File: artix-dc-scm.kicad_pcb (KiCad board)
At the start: 8 copper layers, 90 x 120.4 mm, 342 parts, among them IC1 TPS54561, J1 WE-RJ45_7499111121A, J10 61300611121, J11 DC_SOCKET, J12 S2B-PH-K-S_LF__SN_, J13 62000311121, J2 1-2199230-6, J3 543630489, J4 M20-7830642, J5 SFF-TA-1002-4C+, J6 0878311420, J7 61301021121, J8 61301021121, J9 61301221121, Q1 IRLML6402TRPBF, Q10 2N7002, Q11 2N7002, Q2 IRLML6402TRPBF, Q3 IRLML6402TRPBF, Q4 IRLML6402TRPBF, Q5 IRLML6402TRPBF, Q6 IRLML6402TRPBF, Q7 2N7002, Q8 2N7002, Q9 2N7002, U1 KSZ9031RNXCA, U10 TPS62823DLCT, U11 TPS62823DLCT, U12 TPS62823DLCT, U13 TPS62823DLCT, U14 XC7A100T-FGG484, U15 SN74LVC1G08DCKR, U15 TPS62823DLCT, U16 SN74LS08DBR, U2 W25Q32JVSSIQ_TR, U3 W25Q32JVSSIQ_TR, U4 W25Q32JVSSIQ_TR, U5 W25Q32JVSSIQ_TR, U6 NVT2008DQ,115, U7 AS4C256M16D3, U8 TPS51200DRC, U9 LM3881MME_NOPB, Y1 ABM8G-25.000MHZ-18-D2Y-T

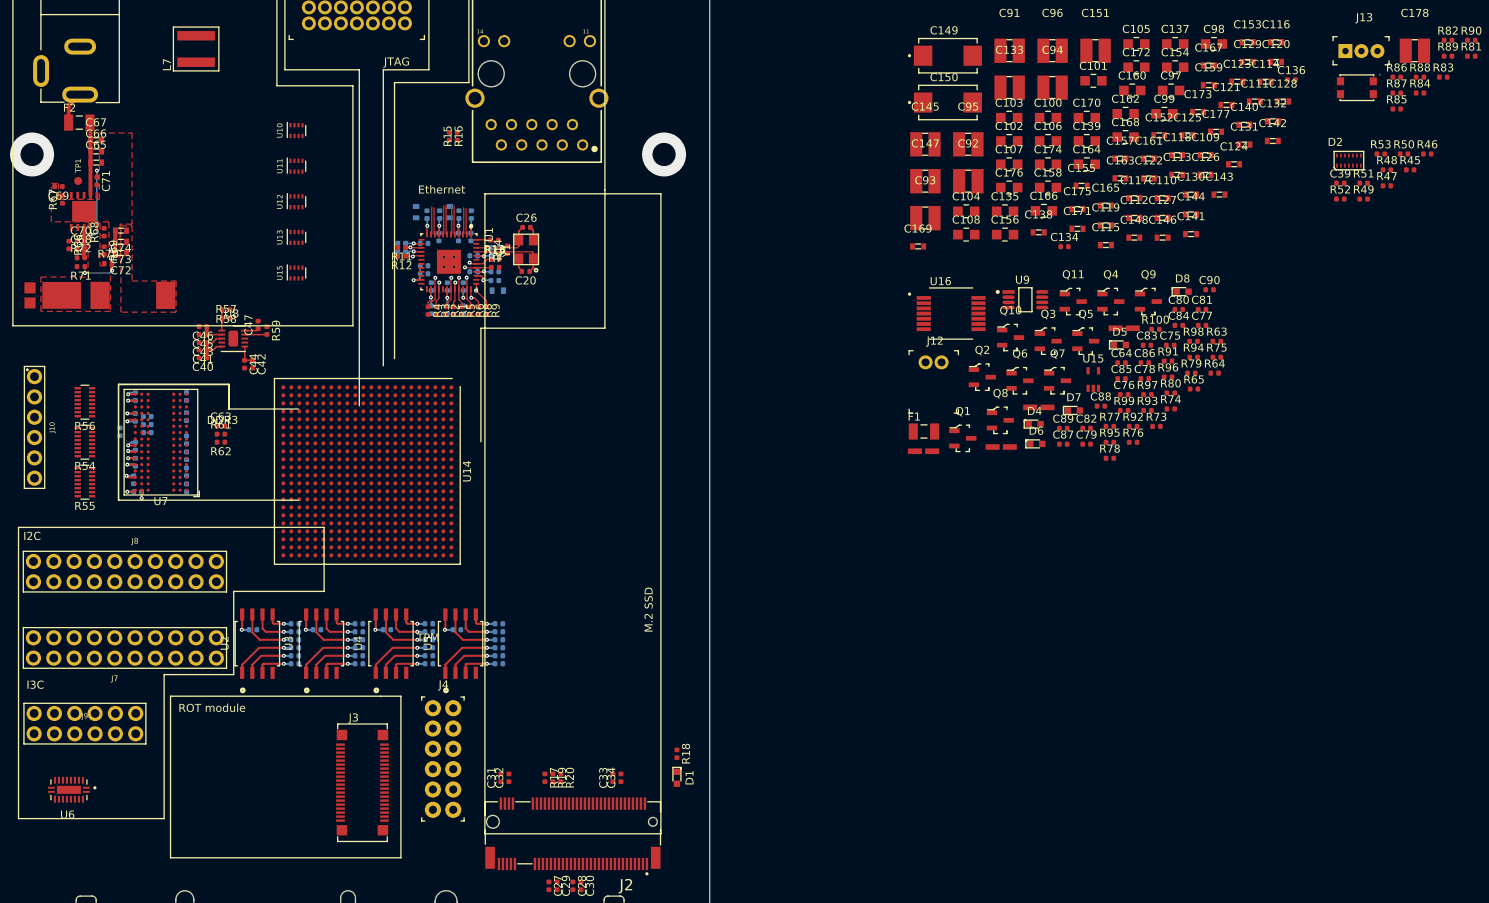
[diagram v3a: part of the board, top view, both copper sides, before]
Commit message: Added interfaces layouts
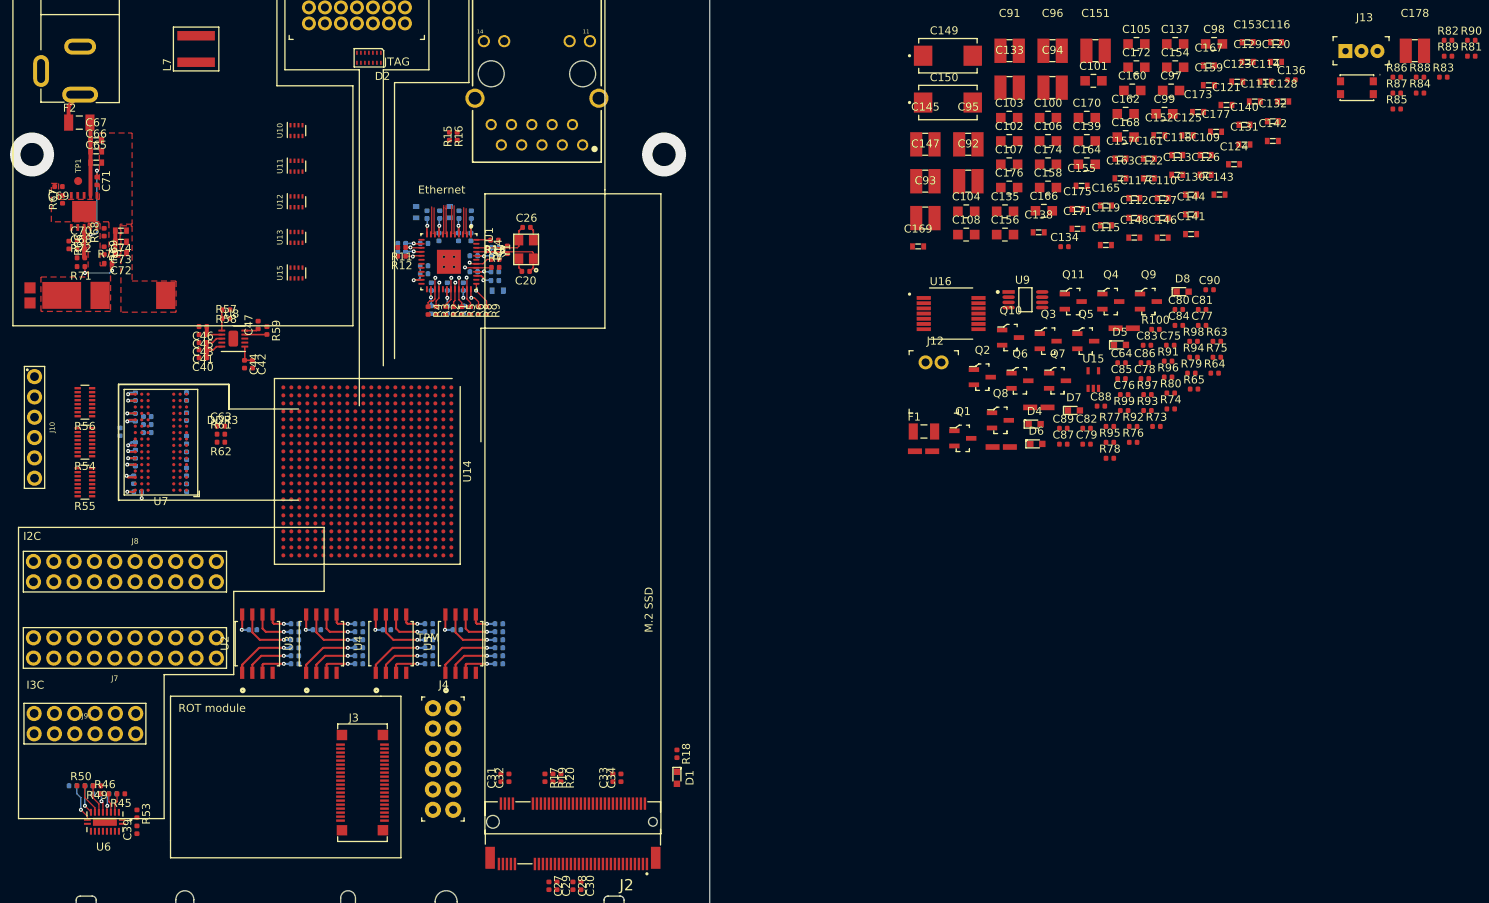
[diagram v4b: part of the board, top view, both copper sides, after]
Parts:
- R47, R48, R51, R52: moved to B.Cu
- moved R46 183.6 mm to (74.5, 160.0)
- moved R50 183.3 mm to (71.5, 159.0)
- moved R48 179.1 mm to (73.5, 160.0)
- moved R45 179.0 mm to (76.5, 160.0), turned to 180 degrees
- moved R47 176.5 mm to (75.5, 160.0), turned to 180 degrees
- moved R51 176.2 mm to (72.5, 159.0), turned to 180 degrees
- moved R53 176.0 mm to (78.5, 162.5), turned to 270 degrees
- moved R52 174.6 mm to (70.5, 159.0)
- moved R49 174.5 mm to (73.5, 159.0), turned to 180 degrees
- moved C39 170.8 mm to (78.5, 164.5), turned to 90 degrees
- moved D2 123.2 mm to (107.5, 68.0), turned to 180 degrees
- moved U6 6.02 mm to (74.5, 163.5)
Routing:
- net I3C[3]_SCL_3V3: track 0.00 -> 4.80 mm, vias 0 -> 1
- net I3C[2]_SCL_3V3: track 0.00 -> 3.84 mm
- net I3C[3]_SDA_3V3: track 0.00 -> 3.63 mm, vias 0 -> 1
- net I3C[2]_SDA_3V3: track 0.00 -> 3.62 mm
- net I3C[1]_SCL_3V3: track 0.00 -> 2.42 mm, vias 0 -> 1
- net I3C[0]_SDA_3V3: track 0.00 -> 2.42 mm
- net I3C[0]_SCL_3V3: track 0.00 -> 2.42 mm
- net I3C[1]_SDA_3V3: track 0.00 -> 2.42 mm, vias 0 -> 1

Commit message: Add local component libraries
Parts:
- C1, C10, C11, C12, C13, C134, C136, C14, C15, C16, C17, C18, C19, C2, C20, C21, C22, C23, C24, C25, C26, C27, C28, C29, C3, C30, C31, C32, C33, C34, C35, C36, C37, C38, C39, C4, C40, C41, C42, C43, C44, C45, C46, C47, C48, C49, C5, C50, C51, C52, C53, C54, C55, C56, C57, C58, C59, C6, C60, C61, C62, C63, C64, C68, C69, C7, C70, C71, C75, C76, C77, C78, C8, C83, C84, C85, C86, C87, C88, C89, C9, C90: footprint antmicro-footprints:0402-cap -> artix-dc-scm-footprints:0402-cap
- C100, C101, C102, C103, C104, C105, C106, C107, C108, C135, C137, C139, C154, C156, C158, C160, C162, C164, C166, C168, C170, C172, C174, C176, C97, C98, C99: footprint antmicro-footprints:0805-cap -> artix-dc-scm-footprints:0805-cap
- C109, C110, C111, C112, C113, C114, C115, C116, C117, C118, C119, C120, C121, C122, C123, C124, C125, C126, C127, C128, C129, C130, C131, C132, C138, C140, C141, C142, C143, C144, C146, C148, C152, C153, C155, C157, C159, C161, C163, C165, C167, C169, C171, C173, C175, C177, C65, C66, C67, C72, C73, C74: footprint antmicro-footprints:0603-cap -> artix-dc-scm-footprints:0603-cap
- C133, C145, C147, C151, C178, C91, C92, C93, C94, C95, C96: footprint antmicro-footprints:1210-cap -> artix-dc-scm-footprints:1210-cap
- C149, C150: footprint antmicro-footprints:KEMET_D -> artix-dc-scm-footprints:KEMET_D
- C79, C80, C81, C82, R1, R10, R100, R11, R12, R13, R14, R15, R16, R17, R18, R19, R2, R20, R21, R22, R23, R24, R25, R26, R27, R28, R29, R3, R30, R31, R32, R33, R34, R35, R36, R37, R38, R39, R4, R40, R41, R42, R43, R44, R45, R46, R47, R48, R49, R5, R50, R51, R52, R53, R57, R58, R59, R6, R60, R61, R62, R63, R64, R65, R66, R67, R68, R69, R7, R70, R71, R72, R73, R74, R75, R76, R77, R78, R79, R8, R80, R81, R82, R83, R84, R85, R86, R87, R88, R89, R9, R90, R91, R92, R93, R94, R95, R96, R97, R98, R99: footprint antmicro-footprints:0402-res -> artix-dc-scm-footprints:0402-res
- D1, D4, D5, D6, D7, D8: footprint antmicro-footprints:LED_0603 -> artix-dc-scm-footprints:LED_0603
- D2: footprint antmicro-footprints:TPD6E05U06 -> artix-dc-scm-footprints:TPD6E05U06
- D3: footprint antmicro-footprints:PDS760-13 -> artix-dc-scm-footprints:PDS760-13
- F1, F2: footprint antmicro-footprints:1206-Fuse-Littelfuse-0466-0-0-MFG -> artix-dc-scm-footprints:1206-Fuse-Littelfuse-0466-0-0-MFG
- FB1, FB2, FB3: footprint antmicro-footprints:0603-res -> artix-dc-scm-footprints:0603-res
- IC1: footprint antmicro-footprints:WSON-10_4x4 -> artix-dc-scm-footprints:WSON-10_4x4
- J1: footprint antmicro-footprints:7499111121A -> artix-dc-scm-footprints:7499111121A
- J10: footprint antmicro-footprints:61300611121 -> artix-dc-scm-footprints:61300611121
- J11: footprint antmicro-footprints:DC_SOCKET -> artix-dc-scm-footprints:DC_SOCKET
- J12: footprint antmicro-footprints:PinHeader_1x2_P2mm_Drill1mm_RA -> artix-dc-scm-footprints:PinHeader_1x2_P2mm_Drill1mm_RA
- J13: footprint antmicro-footprints:62000311121 -> artix-dc-scm-footprints:62000311121
- J2: footprint antmicro-footprints:1-2199230-6 -> artix-dc-scm-footprints:1-2199230-6
- J3: footprint antmicro-footprints:543630489 -> artix-dc-scm-footprints:543630489
- J4: footprint antmicro-footprints:PinHeader_6x2_P2.54mm_Vertical -> artix-dc-scm-footprints:PinHeader_6x2_P2.54mm_Vertical
- J5: footprint antmicro-footprints:SFF-TA-1002-4C+ -> artix-dc-scm-footprints:SFF-TA-1002-4C+
- J6: footprint antmicro-footprints:PinHeader_2x7_P2mm_Drill1mm -> artix-dc-scm-footprints:PinHeader_2x7_P2mm_Drill1mm
- J7, J8: footprint antmicro-footprints:61301021121 -> artix-dc-scm-footprints:61301021121
- J9: footprint antmicro-footprints:61301221121 -> artix-dc-scm-footprints:61301221121
- L1: footprint antmicro-footprints:WE_7447798720 -> artix-dc-scm-footprints:WE_7447798720
- L2, L3, L4, L5: footprint antmicro-footprints:IHLP-1212AE -> artix-dc-scm-footprints:IHLP-1212AE
- L7: footprint antmicro-footprints:Coilcraft-XAL5030 -> artix-dc-scm-footprints:Coilcraft-XAL5030
- Q1, Q10, Q11, Q2, Q3, Q4, Q5, Q6, Q7, Q8, Q9: footprint antmicro-footprints:SOT-23-3 -> artix-dc-scm-footprints:SOT-23-3
- R54, R55, R56: footprint antmicro-footprints:R_Array_Convex_8x0602 -> artix-dc-scm-footprints:R_Array_Convex_8x0602
- S1: footprint antmicro-footprints:SW_SPST_4.2x2.8 -> artix-dc-scm-footprints:SW_SPST_4.2x2.8
- TP1: footprint antmicro-footprints:Testpoint_smd_1mm -> artix-dc-scm-footprints:Testpoint_smd_1mm
- U1: footprint antmicro-footprints:QFN-48-Microchip-QFN77-48LD-PL-2 -> artix-dc-scm-footprints:QFN-48-Microchip-QFN77-48LD-PL-2
- U10, U11, U12, U13, U15: footprint antmicro-footprints:QFN-8_2x1mm -> artix-dc-scm-footprints:QFN-8_2x1mm
- U14: footprint antmicro-footprints:Xilinx_FGG484 -> artix-dc-scm-footprints:Xilinx_FGG484
- U15: footprint antmicro-footprints:SC-70-5 -> artix-dc-scm-footprints:SC-70-5
- U16: footprint antmicro-footprints:SOP65P775X265-14N -> artix-dc-scm-footprints:SOP65P775X265-14N
- U2, U3, U4, U5: footprint antmicro-footprints:W25Q32JVSSIQ -> artix-dc-scm-footprints:W25Q32JVSSIQ
- U6: footprint antmicro-footprints:QFN50P250X450X100-21N -> artix-dc-scm-footprints:QFN50P250X450X100-21N
- U7: footprint antmicro-footprints:BGA-96_9.0x13.0mm_Layout2x3x16_P0.8mm -> artix-dc-scm-footprints:BGA-96_9.0x13.0mm_Layout2x3x16_P0.8mm
- U8: footprint antmicro-footprints:VSON-10-1EP_3x3mm -> artix-dc-scm-footprints:VSON-10-1EP_3x3mm
- U9: footprint antmicro-footprints:VSSOP8-Texas_Instruments-DGK0008A -> artix-dc-scm-footprints:VSSOP8-Texas_Instruments-DGK0008A
- Y1: footprint antmicro-footprints:KX-7 -> artix-dc-scm-footprints:KX-7

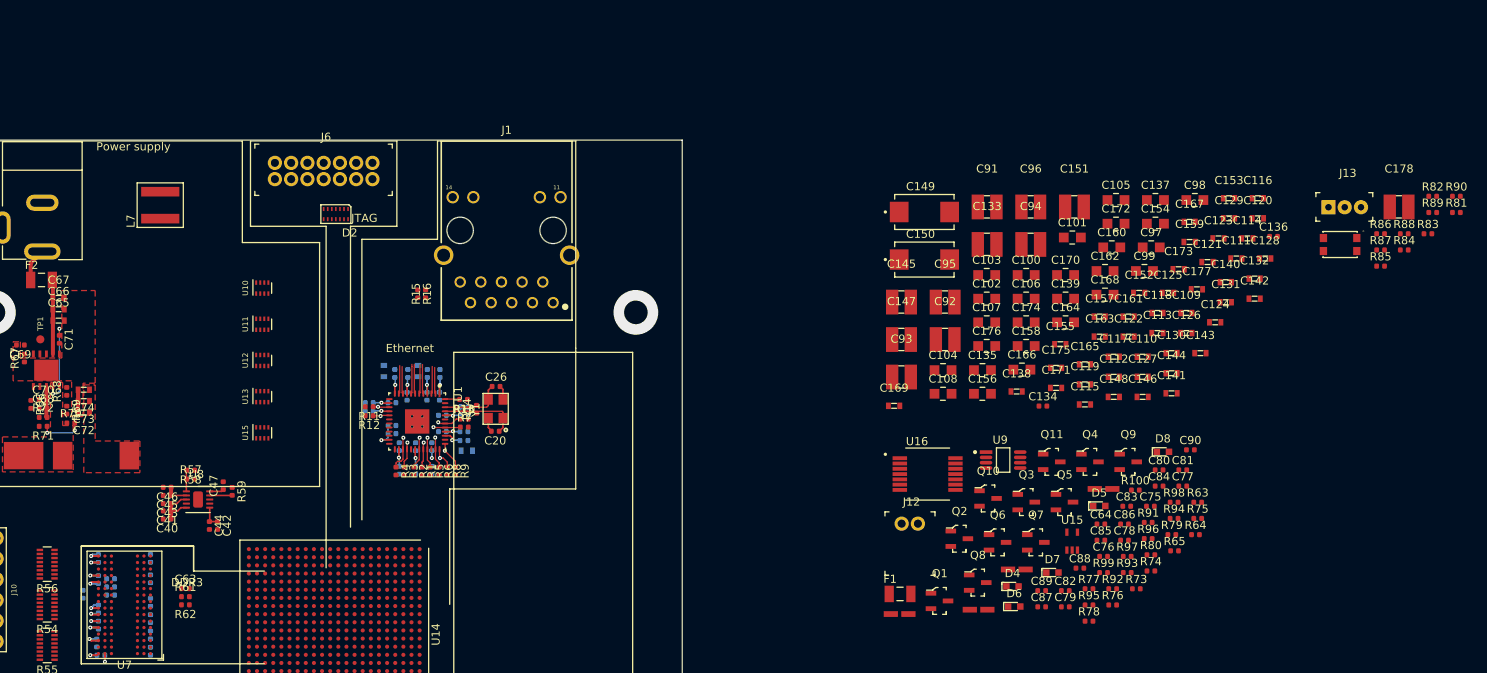
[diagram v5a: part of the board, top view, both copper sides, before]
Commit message: Added VRs component placement, fix in 5V0 layout
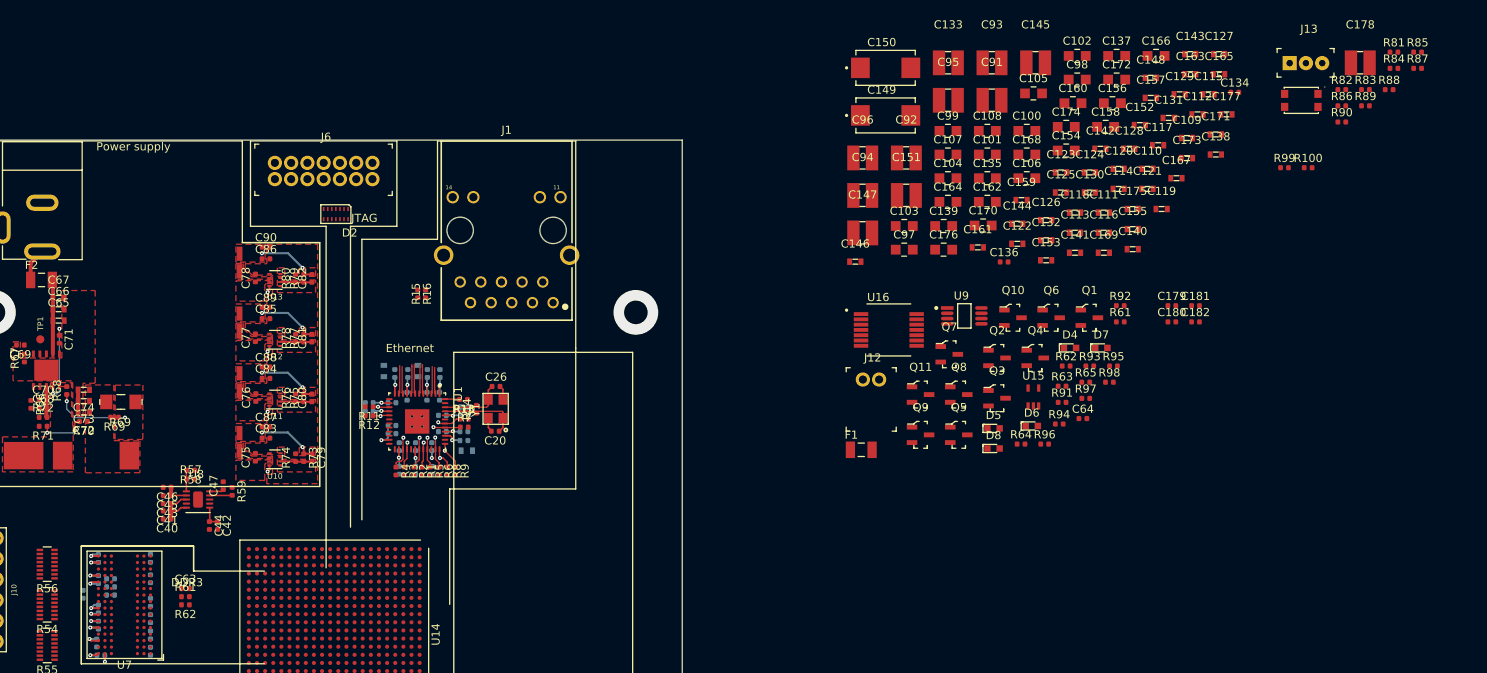
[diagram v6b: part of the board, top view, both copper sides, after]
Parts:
- removed L7: XAL5030-801, artix-dc-scm-footprints:Coilcraft-XAL5030
- removed the R69 at (74.4, 92.1)
- removed the U15 at (198.1, 108.2)
- removed the U15 at (98.5, 94.9)
- added C179: C_100n_0402, artix-dc-scm-footprints:0402-cap, F.Cu at (210.3, 79.3)
- added C180: C_100n_0402, artix-dc-scm-footprints:0402-cap, F.Cu at (210.3, 81.3)
- added C181: C_100n_0402, artix-dc-scm-footprints:0402-cap, F.Cu at (213.2, 79.3)
- added C182: C_100n_0402, artix-dc-scm-footprints:0402-cap, F.Cu at (213.2, 81.3)
- added R61: R_10k_0402, artix-dc-scm-footprints:0402-res, F.Cu at (204.0, 81.3)
- added R62: R_10k_0402, artix-dc-scm-footprints:0402-res, F.Cu at (197.3, 86.7)
- added R69: R_0R_1206, artix-dc-scm-footprints:1206-res, F.Cu at (81.1, 91.1)
- added R69: R_0R_0402, artix-dc-scm-footprints:0402-res, F.Cu at (80.3, 93.0)
- added U15: SN74LVC1G08DCKR, artix-dc-scm-footprints:SC-70-5, F.Cu at (193.3, 90.5)
- R100, R99: value R_1k_0402 -> R_51R_0402
- R94, R95: value R_10k_0402 -> R_1k_0402
- moved C90 116.4 mm to (98.9, 72.1)
- moved C77 115.5 mm to (97.6, 83.2), turned to 90 degrees
- moved C78 111.6 mm to (97.6, 75.9), turned to 90 degrees
- moved R79 111.3 mm to (103.6, 75.9), turned to 90 degrees
- moved R75 110.9 mm to (103.6, 90.6), turned to 90 degrees
- moved C84 110.6 mm to (98.9, 88.2)
- moved R80 110.5 mm to (102.6, 75.9), turned to 90 degrees
- moved C86 110.5 mm to (98.9, 73.5)
- moved C75 110.2 mm to (97.6, 97.9), turned to 90 degrees
- moved L5 109.8 mm to (95.7, 74.0), turned to 90 degrees
- moved C81 108.3 mm to (104.6, 83.3), turned to 90 degrees
- moved C85 106.2 mm to (98.9, 80.9)
- moved C83 106.2 mm to (98.9, 95.6)
- moved R74 106.1 mm to (102.6, 98.0), turned to 90 degrees
- moved C76 106.1 mm to (97.7, 90.6), turned to 90 degrees
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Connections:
- C28 pad 2: Net-(C28-Pad2) -> PCIE_HPM_TXP[1]
- C30 pad 2: Net-(C30-Pad2) -> PCIE_HPM_TXN[1]
- J2 pad 17: Net-(J2-Pad17) -> PCIE_HPM_RXN[2]
- J2 pad 19: Net-(J2-Pad19) -> PCIE_HPM_RXP[2]
- J2 pad 29: Net-(J2-Pad29) -> PCIE_HPM_RXN[1]
- J2 pad 31: Net-(J2-Pad31) -> PCIE_HPM_RXP[1]
- J2 pad 5: Net-(J2-Pad5) -> PCIE_HPM_RXN[3]
- J2 pad 7: Net-(J2-Pad7) -> PCIE_HPM_RXP[3]
- R100 pad 1: Net-(D8-Pad1) -> Net-(C63-Pad2)
- R100 pad 2: VCC3V3 -> DDR3_CLK-
- R91 pad 1: VCC1V0 -> VCC1V8
- R91 pad 2: /Power supply/1V0_PG -> /Power supply/1V8_PG
- R92 pad 1: /Power supply/PWR_EN -> VCC1V35
- R92 pad 2: GND -> /Power supply/1V35_PG
- R93 pad 1: VCC1V8 -> VCC3V3
- R93 pad 2: /Power supply/1V8_PG -> /Power supply/2V5_PG
- R94 pad 1: VCC1V35 -> Net-(D4-Pad1)
- R94 pad 2: /Power supply/1V35_PG -> VCC3V3
- R95 pad 1: VCC3V3 -> Net-(D5-Pad1)
- R95 pad 2: /Power supply/2V5_PG -> VCC3V3
- R96 pad 1: Net-(D4-Pad1) -> Net-(D6-Pad1)
- R97 pad 1: Net-(D5-Pad1) -> Net-(D7-Pad1)
- R98 pad 1: Net-(D6-Pad1) -> Net-(D8-Pad1)
- R99 pad 1: Net-(D7-Pad1) -> DDR3_CLK+
- R99 pad 2: VCC3V3 -> Net-(C63-Pad2)
- U14 pad G13: Net-(U14-PadG13) -> PCIE_BMC_TX_DP
- U14 pad G15: Net-(U14-PadG15) -> PCIE_BMC_TX_DN
- U14 pad G16: Net-(U14-PadG16) -> PCIE_BMC_RX_DP
- U14 pad H13: Net-(U14-PadH13) -> CLK_100M_PCIE_DN
- U14 pad J14: Net-(U14-PadJ14) -> PCIE_BMC_RX_DN
- U14 pad J16: Net-(U14-PadJ16) -> CLK_100M_PCIE_DP
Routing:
- net (no net): track 0.00 -> 11.7 mm
- net VCC5V0: track 0.00 -> 9.69 mm, vias 0 -> 2
- net Net-(C80-Pad2): track 0.00 -> 7.62 mm, vias 0 -> 2
- net Net-(C82-Pad2): track 0.00 -> 7.62 mm, vias 0 -> 2
- net Net-(C81-Pad2): track 0.00 -> 7.62 mm, vias 0 -> 2
- net VCC3V3: track 20.1 -> 27.7 mm, vias 7 -> 9
- net Net-(C79-Pad2): track 0.00 -> 3.89 mm
- net PWR_GOOD: track 0.00 -> 0.91 mm
- net /Power supply/3V3_PG: track 0.00 -> 0.84 mm, vias 0 -> 1
- net /Power supply/1V0_PG: track 0.00 -> 0.84 mm, vias 0 -> 1
- net /Power supply/1V8_PG: track 0.00 -> 0.84 mm, vias 0 -> 1
- net /Power supply/1V35_PG: track 0.00 -> 0.84 mm, vias 0 -> 1
- net Net-(R70-Pad2): track 5.24 -> 5.91 mm
- added copper zone on F.Cu, net Net-(L2-Pad1)
- added copper zone on F.Cu, net Net-(L3-Pad1)
- added copper zone on F.Cu, net Net-(L4-Pad1)
- added copper zone on F.Cu, net Net-(L5-Pad1)
- added copper zone on F.Cu, net VCC1V0
- added copper zone on F.Cu, net VCC1V35
- added copper zone on F.Cu, net VCC1V8
- added copper zone on F.Cu, net VCC3V3
- added copper zone on F.Cu, net VCC5V0
